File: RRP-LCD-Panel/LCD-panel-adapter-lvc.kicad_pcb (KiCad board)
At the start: 2 copper layers, 40.6 x 48.3 mm, 8 parts, among them J101 HEADER_18, P101 CONN_4X2, P102 CONN_5X2, P103 CONN_5X2, U101 SN74LVCC4245A

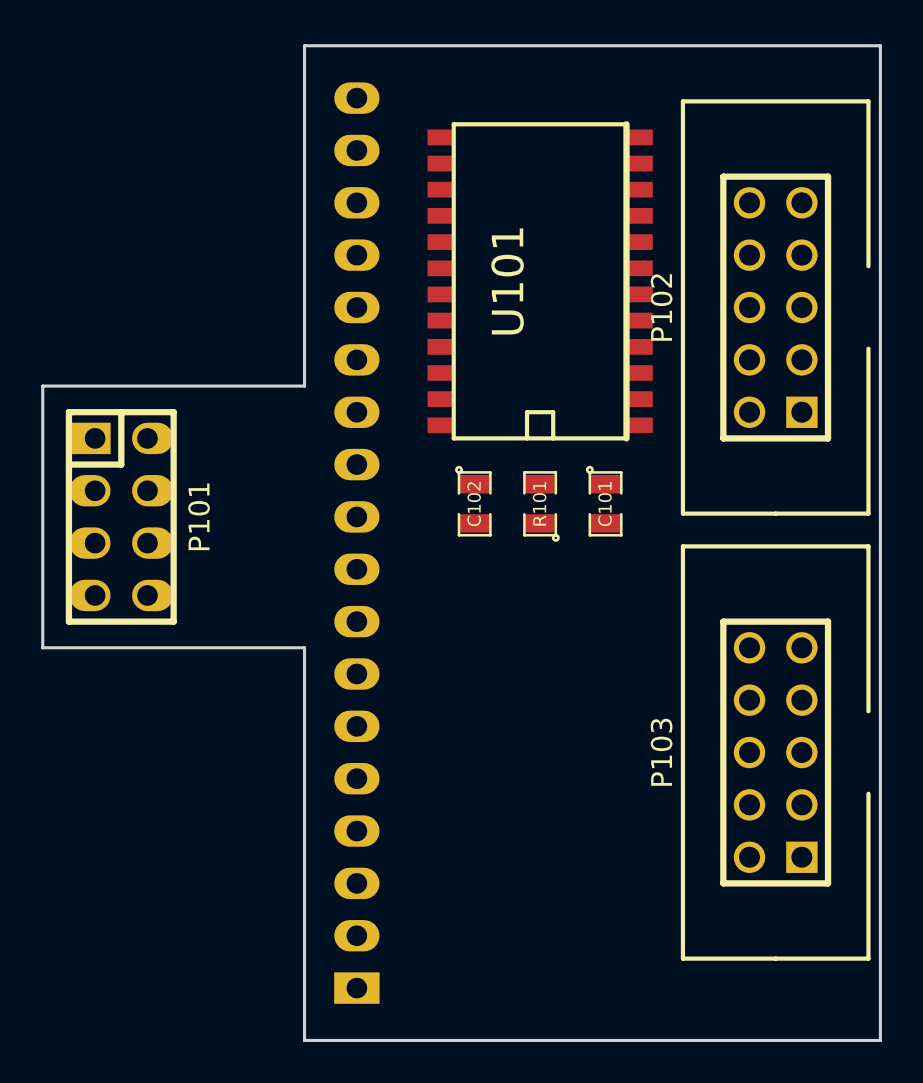
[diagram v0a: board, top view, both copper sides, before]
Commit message: LCD Panel adapter: use 74HC07
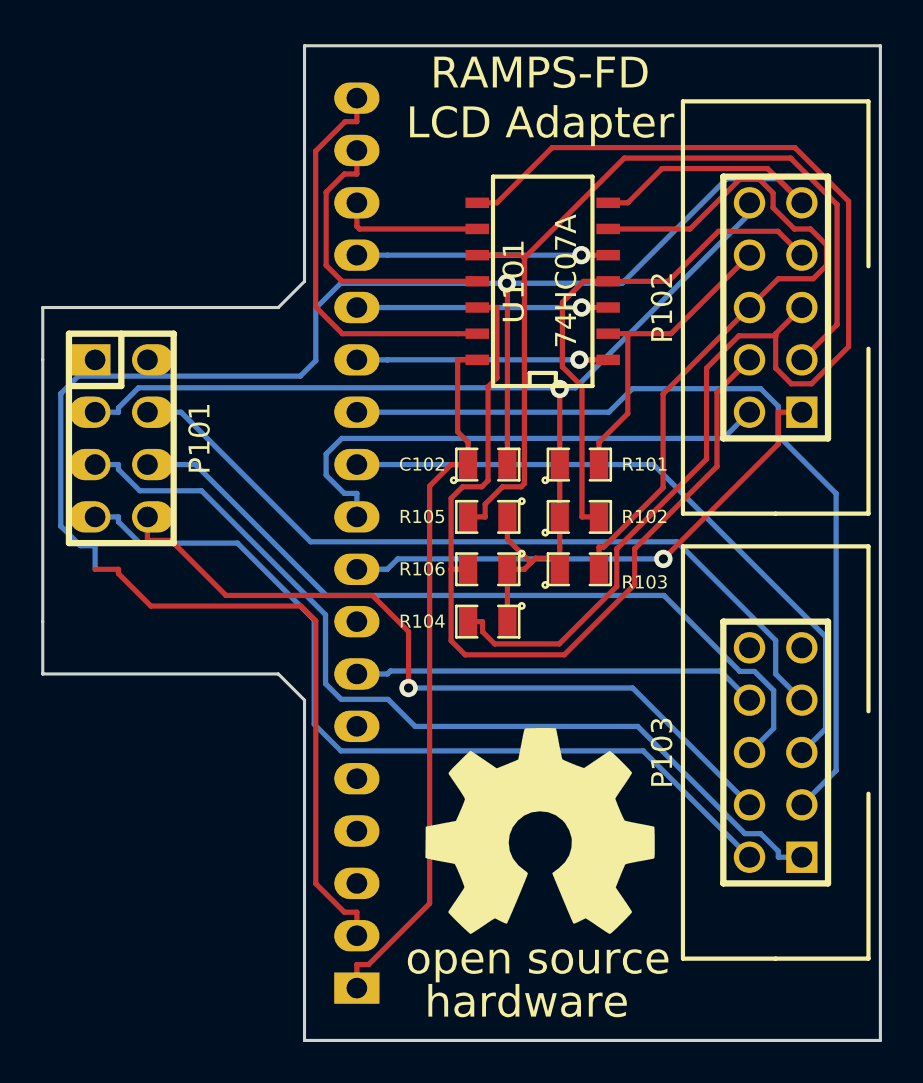
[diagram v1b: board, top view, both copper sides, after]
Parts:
- removed C101: 100nF, SM0805
- added M101: LOGO_OSHW, OSHW_logo_2, F.Cu at (158.8, 110.5)
- added R102: 10k, SM0805, F.Cu at (160.7, 95.2)
- added R103: 10k, SM0805, F.Cu at (160.7, 97.8)
- added R104: 10k, SM0805, F.Cu at (156.2, 100.3)
- added R105: 10k, SM0805, F.Cu at (156.2, 95.2)
- added R106: 10k, SM0805, F.Cu at (156.2, 97.8)
- R101: value 1k -> 10k
- U101: value SN74LVCC4245A -> 74HC07A; footprint SO24E -> SO14N
- moved P101 3.81 mm to (138.4, 91.4)
- moved R101 2.69 mm to (160.7, 92.7), turned to 0 degrees
- moved C102 2.01 mm to (156.2, 92.7), turned to 0 degrees
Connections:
- P102 pad 1: /BEEP_5V -> /BEEP
- R101 pad 1: GND -> +5V
- R101 pad 2: N-0000012 -> /LCD_D7_5V
- U101 pad 1: +5V -> /LCD_D7
- U101 pad 10: (no net) -> /LCD_E_5V
- U101 pad 11: GND -> /LCD_E
- U101 pad 12: GND -> /LCD_RS_5V
- U101 pad 13: GND -> /LCD_RS
- U101 pad 14: N-0000012 -> /IOREF
- U101 pad 2: GND -> /LCD_D7_5V
- U101 pad 3: /BEEP_5V -> /LCD_D6
- U101 pad 4: /LCD_D7_5V -> /LCD_D6_5V
- U101 pad 5: /LCD_D6_5V -> /LCD_D5
- U101 pad 7: /LCD_D4_5V -> GND
- U101 pad 8: /LCD_E_5V -> /LCD_D4_5V
- U101 pad 9: /LCD_RS_5V -> /LCD_D4
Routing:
- net GND: track 0.00 -> 99.8 mm, vias 0 -> 1
- net /LCD_D4_5V: track 0.00 -> 60.8 mm
- net +5V: track 0.00 -> 53.2 mm, vias 0 -> 1
- net /SD_DO: track 0.00 -> 44.4 mm
- net /LCD_E_5V: track 0.00 -> 43.4 mm
- net /LCD_RS_5V: track 0.00 -> 43.2 mm
- net /ENC2: track 0.00 -> 42.5 mm
- net /SD_CLK: track 0.00 -> 41.7 mm
- net /SD_DETECT: track 0.00 -> 38.5 mm
- net /SD_DI: track 0.00 -> 38.4 mm
- net /SD_CS: track 0.00 -> 37.3 mm, vias 0 -> 1
- net /LCD_D5_5V: track 0.00 -> 34.8 mm
- net /IOREF: track 0.00 -> 34.7 mm
- net /ENC1: track 0.00 -> 32.3 mm
- net /BEEP: track 0.00 -> 25.6 mm, vias 0 -> 1
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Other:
- outline, holes or cut-outs redrawn
- board text added: "Assembly notes: 1. P101 and J101 should be mounted on bottom side of PCB."
- board text added: "RAMPS-FD LCD Adapter"
- board text removed: "Assembly notes: 1. P101 should be mounted on bottom side of PCB."
